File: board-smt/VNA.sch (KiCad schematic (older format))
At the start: 111 parts, among them J1 Conn_02x07_Odd_Even, J10 Conn_01x01, J11 Conn_01x01, J12 Conn_01x01, J13 Barrel_Jack, J14 Conn_01x01, J15 Conn_01x02, J16 Conn_01x01, J17 Conn_01x04, J18 Conn_01x01, J19 Conn_01x01, J2 Conn_Coaxial, J20 Conn_01x01, J21 Conn_01x01, J22 Conn_01x02, J24 USB_B, J3 Conn_01x01, J4 Conn_01x01, J5 Conn_01x01, J6 Conn_01x01, J7 Conn_01x01, J8 Conn_01x01, J9 Conn_Coaxial, Q3 S9018, SW1 SW_DPDT_x2, U1 SI5351A, U10 MT3608, U11 CN3052, U12 SI5351A, U8 AMS1117-3V3, U9 78M05_TO252, Y1 27 MHz

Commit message: Changed Schottky diode to SS14 and 1N4148 to BAV99
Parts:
- removed D1, D2, D3, D4: 1N4148, Diodes_SMD:D_SOD-123, symbol D
- added D1, D2: BAV99, TO_SOT_Packages_SMD:SOT-23, symbol D_x2_Serial_AKC
- D5: value D_Schottky -> SS14; footprint Diodes_SMD:D_SOD-123 -> Diodes_SMD:D_SMA
- L10: value L_Small -> 10 uH
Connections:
- wire segments 335 -> 339
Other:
- moved on the sheet: J3, JP3

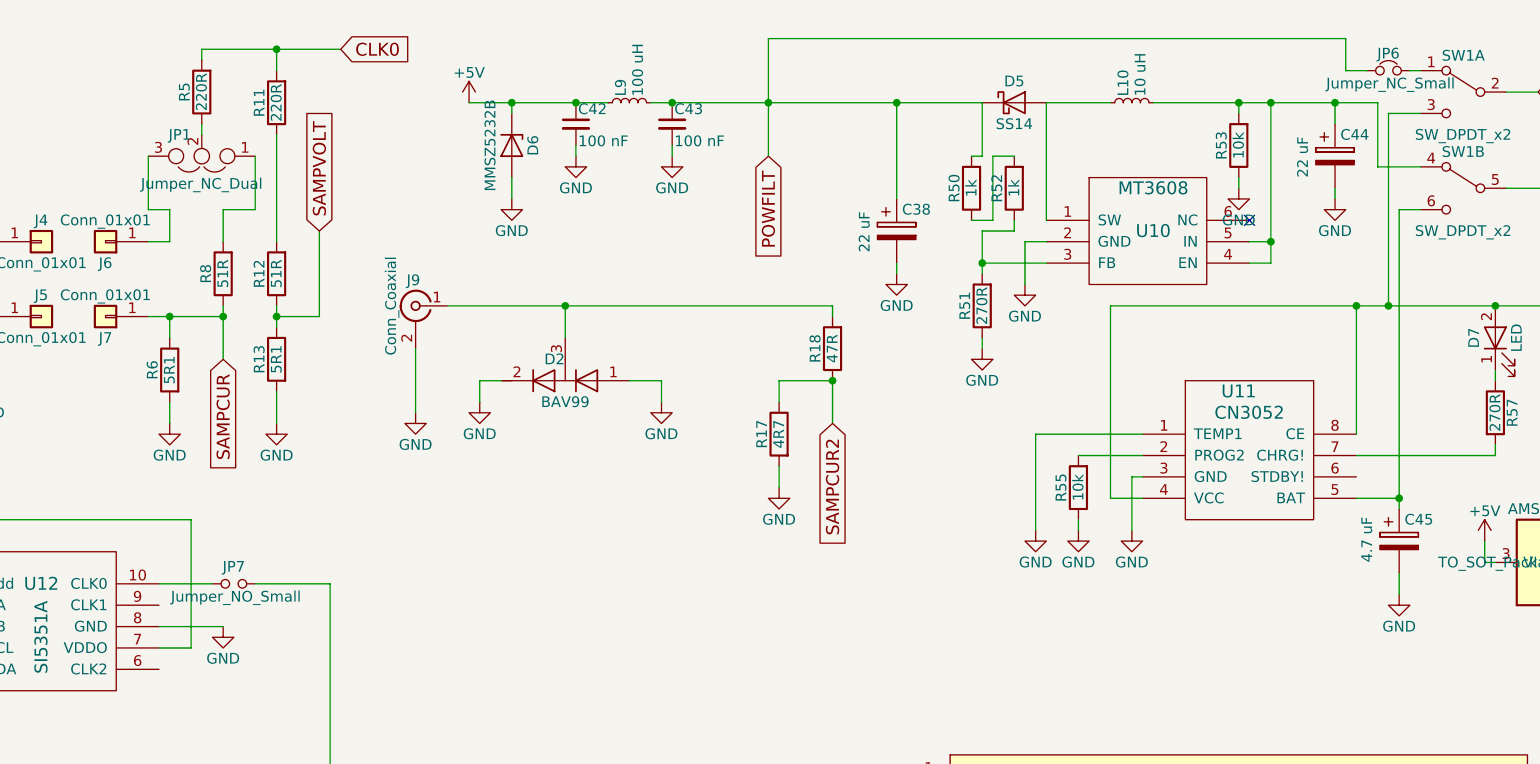
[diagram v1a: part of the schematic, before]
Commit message: Added source termination resistor to LO SI5351A
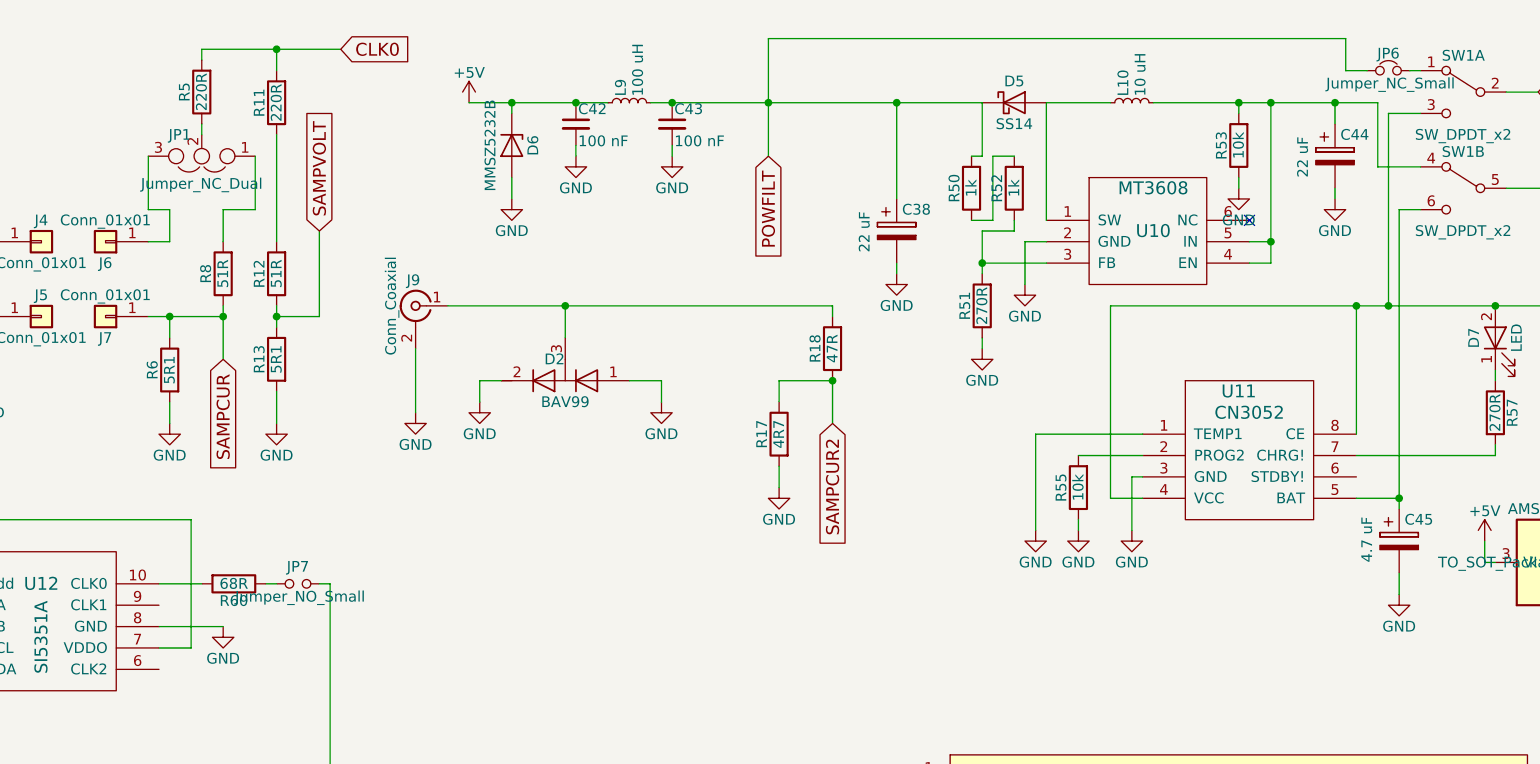
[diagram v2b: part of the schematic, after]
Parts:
- added R60: 68R, Resistors_SMD:R_0805_HandSoldering, symbol R
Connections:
- net at U12.10 (CLK0): now also R60.2; no longer JP7.1
- new net: JP7.1, R60.1
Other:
- moved on the sheet: JP7

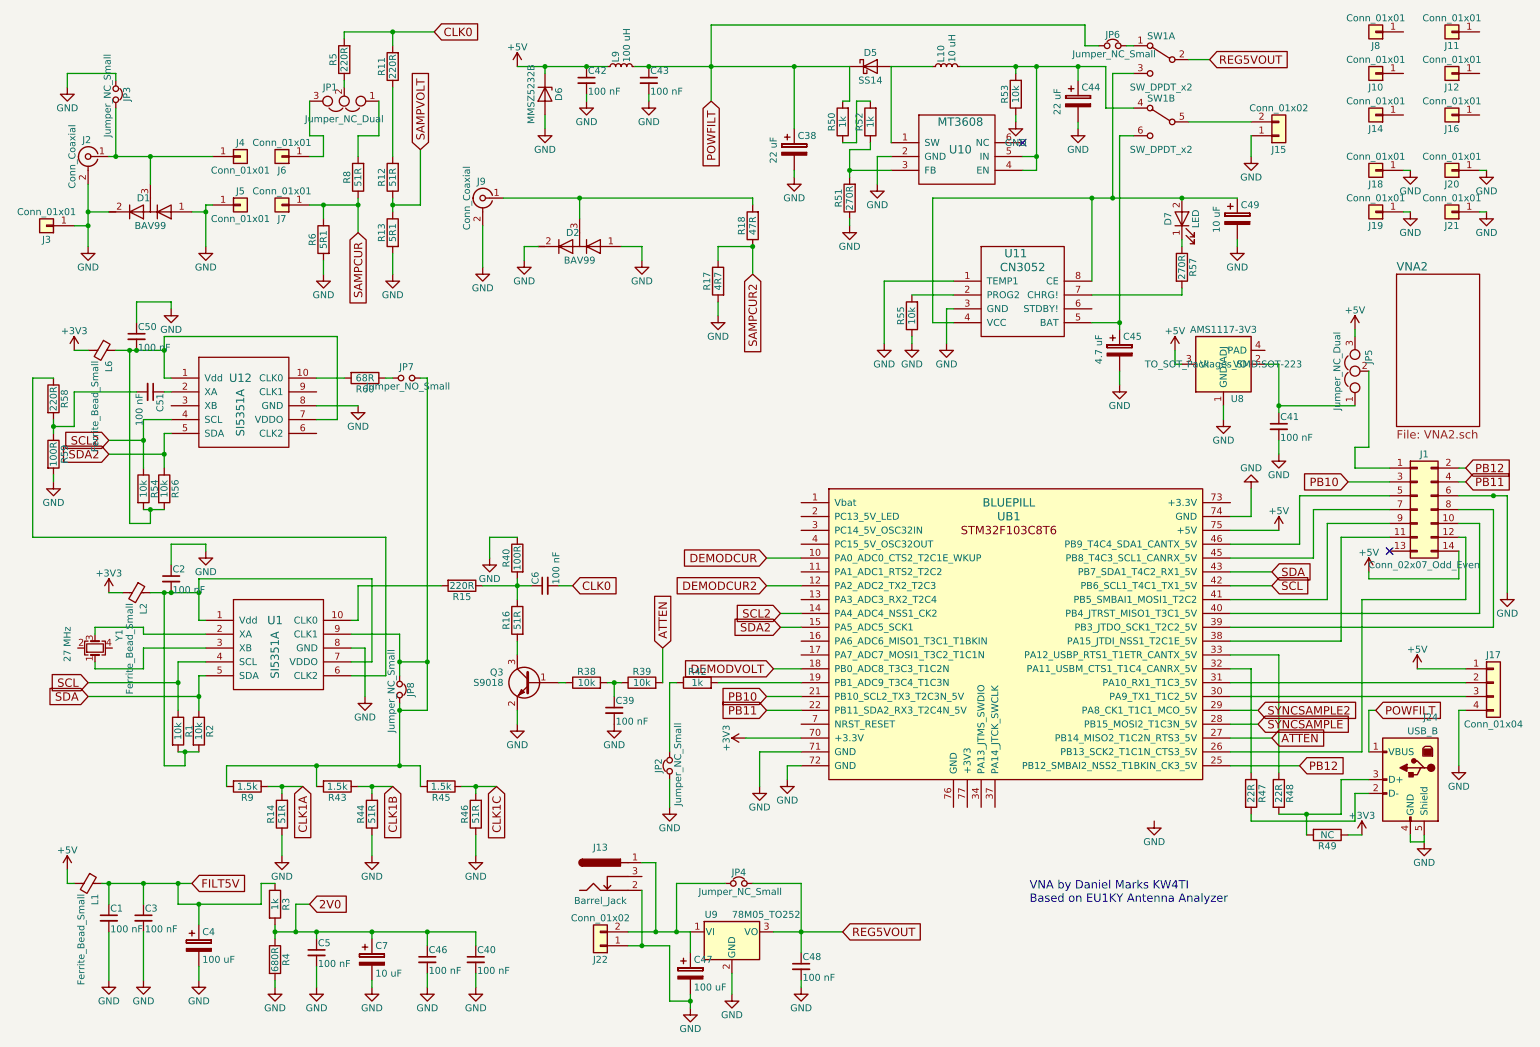
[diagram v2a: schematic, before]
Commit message: Changes to finalize two SI5351A solution
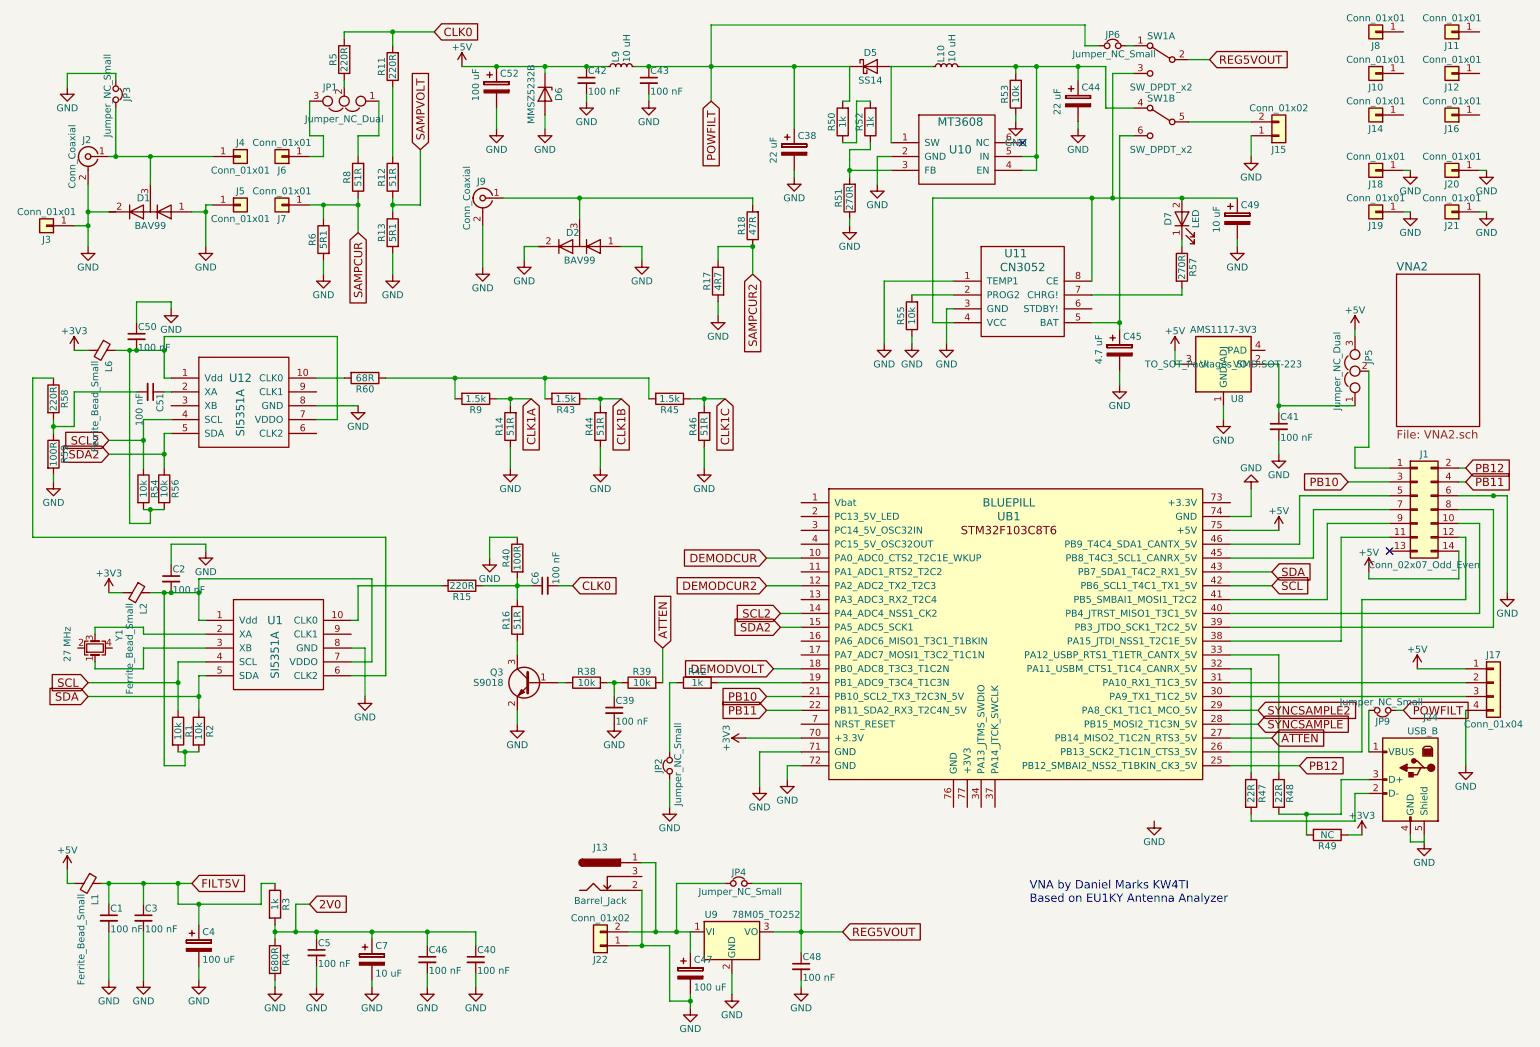
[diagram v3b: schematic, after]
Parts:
- removed JP7: Jumper_NO_Small, VNA:PAD_DEFAULT_OPEN, symbol Jumper_NO_Small
- removed JP8: Jumper_NC_Small, VNA:PAD_DEFAULT_OPEN, symbol Jumper_NC_Small
- added C52: 100 uF, Capacitors_SMD:CP_Elec_4x4.5, symbol CP
- added JP9: Jumper_NC_Small, Pin_Headers:Pin_Header_Straight_1x02_Pitch2.54mm, symbol Jumper_NC_Small
- L9: value 100 uH -> 10 uH
- Y1: footprint (none) -> Crystals:Crystal_SMD_3225-4pin_3.2x2.5mm_HandSoldering
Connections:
- net +5V: now also C52.1
- net GND: now also C52.2
- net POWFILT: now also JP9.1; no longer J24.1 (VBUS)
- net at R43.2, R45.2, R9.2: now also R60.1; no longer U1.9 (CLK1)
- new net: J24.1 (VBUS), JP9.2
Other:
- moved on the sheet: R14, R43, R44, R45, R46, R9

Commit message: Shrank the SMT board by 15 mm
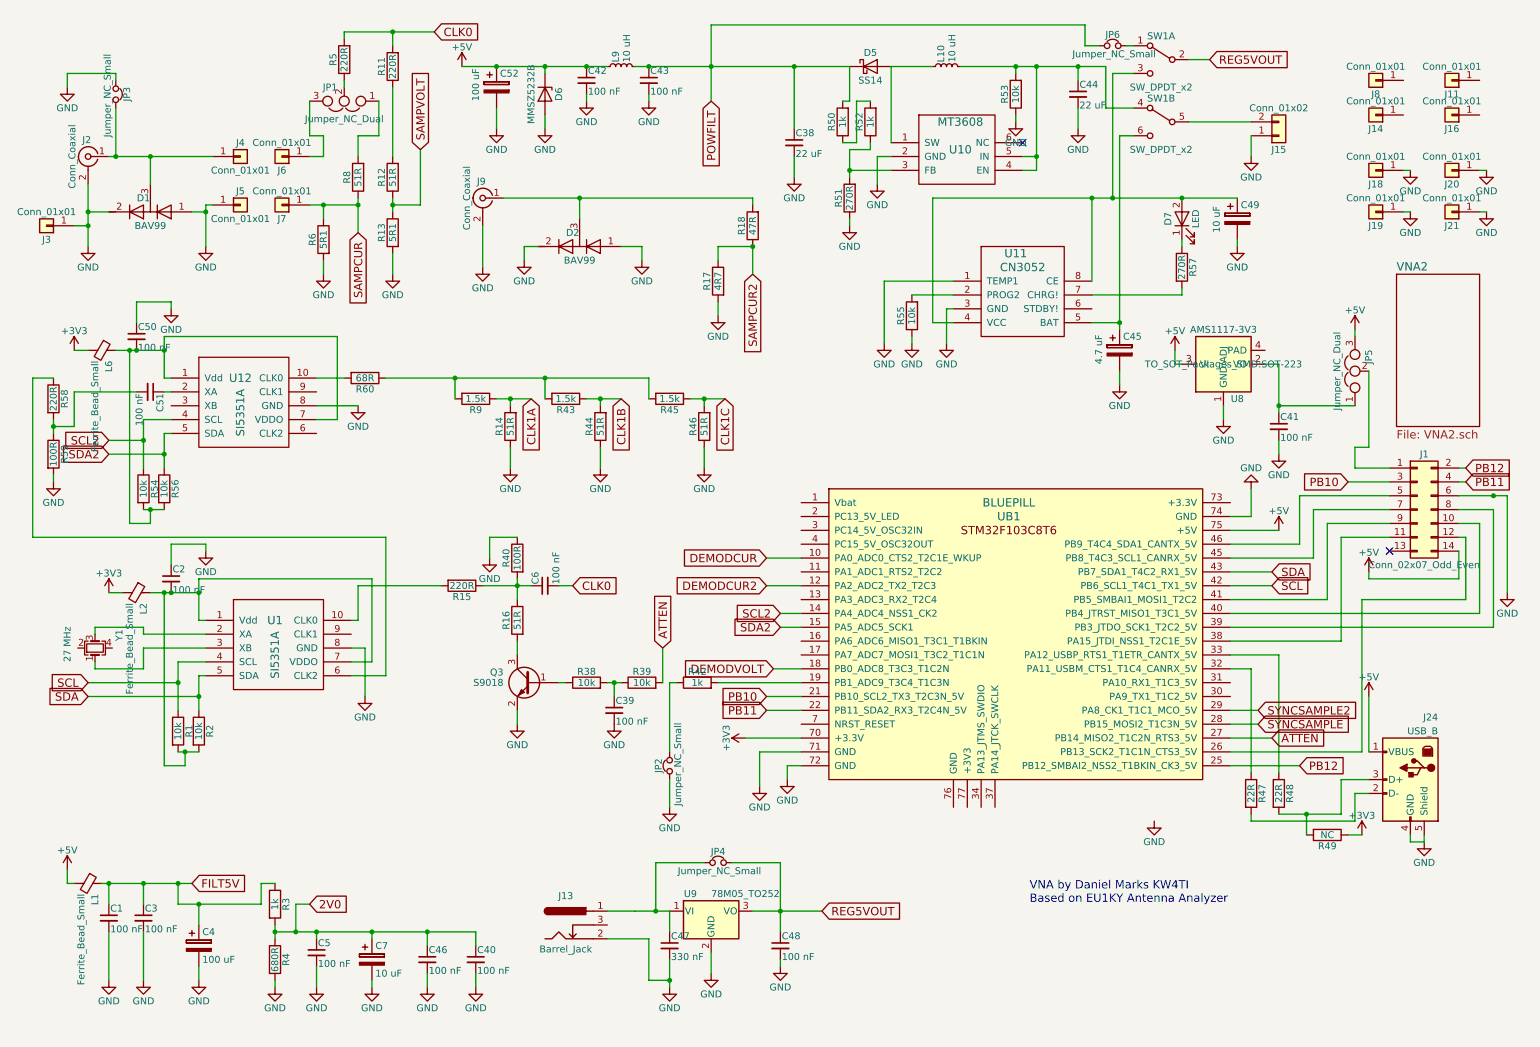
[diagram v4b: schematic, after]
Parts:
- removed C38, C44: 22 uF, Capacitors_SMD:CP_Elec_4x4.5, symbol CP
- removed C47: 100 uF, Capacitors_SMD:CP_Elec_5x5.3, symbol CP
- removed J10, J12: Conn_01x01, Connectors:1pin, symbol Conn_01x01
- removed J17: Conn_01x04, Pin_Headers:Pin_Header_Straight_1x04_Pitch2.54mm, symbol Conn_01x04
- removed J22: Conn_01x02, Connectors_Terminal_Blocks:TerminalBlock_bornier-2_P5.08mm, symbol Conn_01x02
- removed JP9: Jumper_NC_Small, Pin_Headers:Pin_Header_Straight_1x02_Pitch2.54mm, symbol Jumper_NC_Small
- added C38, C44: 22 uF, Capacitors_SMD:C_1210_HandSoldering, symbol C_Small
- added C47: 330 nF, Capacitors_SMD:C_1206_HandSoldering, symbol C_Small
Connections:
- net +5V: now also J24.1 (VBUS)
- net GND: now also C38.2, C44.2, C47.2
- net POWFILT: now also C38.1
- net at J13.1, JP4.1, U9.1 (VI): now also C47.1
- net at L10.2, R53.2, SW1.4 (A)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: now also C44.1
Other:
- moved on the sheet: C48, J11, J13, J8, JP4, U9
